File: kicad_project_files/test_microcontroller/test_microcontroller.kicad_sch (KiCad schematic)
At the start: 40 parts, among them J1 USB_C_Receptacle_USB2.0, SW1 SW_Push, SW2 SW_Push, SW3 SW_Push, SW4 SW_Push, SW5 SW_Push, SW6 SW_Push, SW7 SW_Push, SW8 SW_Push, SW9 SW_Push, U1 ATmega32U4-A, Y1 16mhz

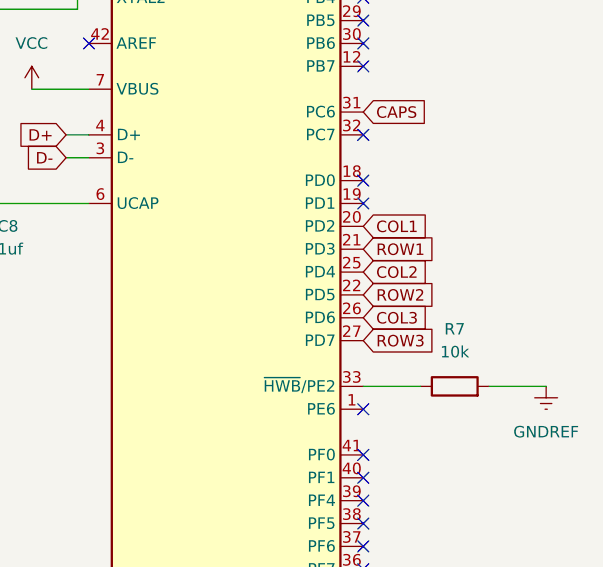
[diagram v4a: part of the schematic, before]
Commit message: add pcb traces
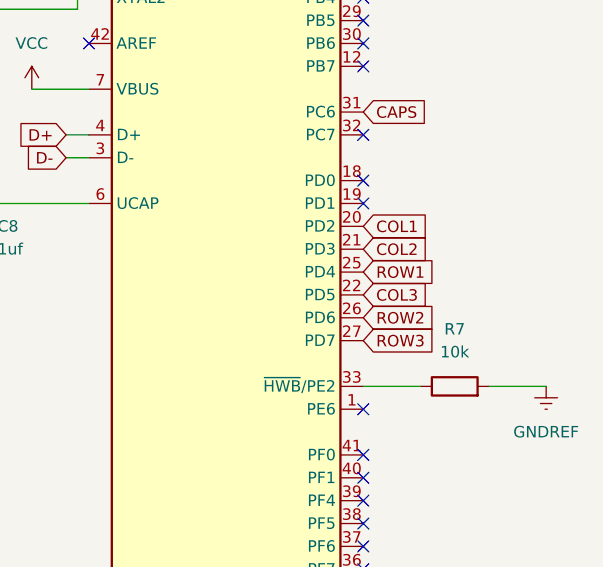
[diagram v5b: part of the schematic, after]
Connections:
- net COL2: now also U1.21 (PD3); no longer U1.25 (PD4)
- net COL3: now also U1.22 (PD5); no longer U1.26 (PD6)
- net ROW1: now also U1.25 (PD4); no longer U1.21 (PD3)
- net ROW2: now also U1.26 (PD6); no longer U1.22 (PD5)
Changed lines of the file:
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@@
+    )
+  )
+  (global_label "COL3" (shape input) (at 246.38 92.71 0) (fields_autoplaced)
+    (effects (font (size 1.27 1.27)) (justify left))
+    (property "Intersheet References" "${INTERSHEET_REFS}" (id 0) (at 253.6312 92.6306 0)
+      (effects (font (size 1.27 1.27)) (justify left) hide)
     )
   )
@@
     (effects (font (size 1.27 1.27)) (justify left))
     (property "Intersheet References" "${INTERSHEET_REFS}" (id 0) (at 183.0555 88.8206 0)
+      (effects (font (size 1.27 1.27)) (justify left) hide)
+    )
+  )
+  (global_label "ROW2" (shape input) (at 246.38 95.25 0) (fields_autoplaced)
+    (effects (font (size 1.27 1.27)) (justify left))
+    (property "Intersheet References" "${INTERSHEET_REFS}" (id 0) (at 254.0545 95.3294 0)
       (effects (font (size 1.27 1.27)) (justify left) hide)
     )
@@
     )
   )
-  (global_label "COL3" (shape input) (at 246.38 95.25 0) (fields_autoplaced)
-    (effects (font (size 1.27 1.27)) (justify left))
-    (property "Intersheet References" "${INTERSHEET_REFS}" (id 0) (at 253.6312 95.1706 0)
-      (effects (font (size 1.27 1.27)) (justify left) hide)
-    )
-  )
   (global_label "ROW2" (shape input) (at 33.02 128.27 180) (fields_autoplaced)
     (effects (font (size 1.27 1.27)) (justify right))
@@
     )
   )
-  (global_label "ROW2" (shape input) (at 246.38 92.71 0) (fields_autoplaced)
-    (effects (font (size 1.27 1.27)) (justify left))
-    (property "Intersheet References" "${INTERSHEET_REFS}" (id 0) (at 254.0545 92.7894 0)
-      (effects (font (size 1.27 1.27)) (justify left) hide)
-    )
-  )
   (global_label "D+" (shape input) (at 177.8 93.98 0) (fields_autoplaced)
     (effects (font (size 1.27 1.27)) (justify left))
@@
     (effects (font (size 1.27 1.27)) (justify left))
     (property "Intersheet References" "${INTERSHEET_REFS}" (id 0) (at 48.1806 76.5688 90)
+      (effects (font (size 1.27 1.27)) (justify left) hide)
+    )
+  )
+  (global_label "COL2" (shape input) (at 246.38 87.63 0) (fields_autoplaced)
+    (effects (font (size 1.27 1.27)) (justify left))
+    (property "Intersheet References" "${INTERSHEET_REFS}" (id 0) (at 253.6312 87.5506 0)
+      (effects (font (size 1.27 1.27)) (justify left) hide)
+    )
+  )
+  (global_label "ROW1" (shape input) (at 246.38 90.17 0) (fields_autoplaced)
+    (effects (font (size 1.27 1.27)) (justify left))
+    (property "Intersheet References" "${INTERSHEET_REFS}" (id 0) (at 254.0545 90.2494 0)
       (effects (font (size 1.27 1.27)) (justify left) hide)
     )
@@
     (effects (font (size 1.27 1.27)) (justify left))
     (property "Intersheet References" "${INTERSHEET_REFS}" (id 0) (at 253.3893 57.0706 0)
-      (effects (font (size 1.27 1.27)) (justify left) hide)
-    )
-  )
-  (global_label "ROW1" (shape input) (at 246.38 87.63 0) (fields_autoplaced)
-    (effects (font (size 1.27 1.27)) (justify left))
-    (property "Intersheet References" "${INTERSHEET_REFS}" (id 0) (at 254.0545 87.7094 0)
-      (effects (font (size 1.27 1.27)) (justify left) hide)
-    )
-  )
-  (global_label "COL2" (shape input) (at 246.38 90.17 0) (fields_autoplaced)
-    (effects (font (size 1.27 1.27)) (justify left))
-    (property "Intersheet References" "${INTERSHEET_REFS}" (id 0) (at 253.6312 90.0906 0)
       (effects (font (size 1.27 1.27)) (justify left) hide)
     )
@@
   (symbol (lib_id "power:PWR_FLAG") (at 148.59 115.57 0) (unit 1)
     (in_bom yes) (on_board yes) (fields_autoplaced)
-    (property "Reference" "#FLG?" (id 0) (at 148.59 113.665 0)
+    (property "Reference" "#FLG0102" (id 0) (at 148.59 113.665 0)
       (effects (font (size 1.27 1.27)) hide)
     )
@@
   (symbol (lib_id "power:PWR_FLAG") (at 158.75 69.85 0) (unit 1)
     (in_bom yes) (on_board yes) (fields_autoplaced)
-    (property "Reference" "#FLG?" (id 0) (at 158.75 67.945 0)
+    (property "Reference" "#FLG0101" (id 0) (at 158.75 67.945 0)
       (effects (font (size 1.27 1.27)) hide)
     )
@@
   )
   (symbol_instances
+    (path "/910bf9c7-3f9b-4ebb-810c-f11944d95f58"
+      (reference "#FLG0101") (unit 1) (value "PWR_FLAG") (footprint "")
+    )
     (path "/4d3913c1-6eaf-4788-b16d-404de55aea6d"
-      (reference "#FLG?") (unit 1) (value "PWR_FLAG") (footprint "")
-    )
-    (path "/910bf9c7-3f9b-4ebb-810c-f11944d95f58"
-      (reference "#FLG?") (unit 1) (value "PWR_FLAG") (footprint "")
+      (reference "#FLG0102") (unit 1) (value "PWR_FLAG") (footprint "")
     )
     (path "/51f6aabe-8284-47cf-8ddc-0d885dfc999b"

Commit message: complete traces
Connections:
- net GNDREF: now also ICSP_Programmer1.2 (Pin_2); no longer ICSP_Programmer1.6 (Pin_6)
- net MOSI: now also ICSP_Programmer1.3 (Pin_3); no longer ICSP_Programmer1.4 (Pin_4)
- net RESET: now also ICSP_Programmer1.4 (Pin_4); no longer ICSP_Programmer1.5 (Pin_5)
- net SCLK: now also ICSP_Programmer1.5 (Pin_5); no longer ICSP_Programmer1.3 (Pin_3)
- net VCC: now also ICSP_Programmer1.6 (Pin_6); no longer ICSP_Programmer1.2 (Pin_2)
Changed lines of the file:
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@@
   (no_connect (at 246.38 105.41))
   (no_connect (at 246.38 49.53))
-  (wire (pts (xy 130.81 50.8) (xy 130.81 52.07))
+  (wire (pts (xy 130.81 50.8) (xy 130.81 54.61))
     (stroke (width 0) (type default) (color 0 0 0 0))
   )
@@
     (stroke (width 0) (type default) (color 0 0 0 0))
   )
+  (wire (pts (xy 139.7 54.61) (xy 130.81 54.61))
+    (stroke (width 0) (type default) (color 0 0 0 0))
+  )
   (wire (pts (xy 36.83 29.21) (xy 40.64 29.21))
     (stroke (width 0) (type default) (color 0 0 0 0))
@@
     (stroke (width 0) (type default) (color 0 0 0 0))
   )
+  (wire (pts (xy 128.27 41.91) (xy 128.27 45.72))
+    (stroke (width 0) (type default) (color 0 0 0 0))
+  )
   (wire (pts (xy 33.02 149.86) (xy 38.1 149.86))
     (stroke (width 0) (type default) (color 0 0 0 0))
@@
     (stroke (width 0) (type default) (color 0 0 0 0))
   )
+  (wire (pts (xy 138.43 41.91) (xy 128.27 41.91))
+    (stroke (width 0) (type default) (color 0 0 0 0))
+  )
   (wire (pts (xy 134.62 113.03) (xy 134.62 116.84))
     (stroke (width 0) (type default) (color 0 0 0 0))
@@
   )
   (wire (pts (xy 163.83 90.17) (xy 163.83 88.9))
-    (stroke (width 0) (type default) (color 0 0 0 0))
-  )
-  (wire (pts (xy 128.27 45.72) (xy 133.35 45.72))
     (stroke (width 0) (type default) (color 0 0 0 0))
   )
@@
     )
   )
-  (global_label "SCLK" (shape input) (at 115.57 48.26 180) (fields_autoplaced)
-    (effects (font (size 1.27 1.27)) (justify right))
-    (property "Intersheet References" "${INTERSHEET_REFS}" (id 0) (at 108.3793 48.3394 0)
-      (effects (font (size 1.27 1.27)) (justify right) hide)
-    )
-  )
   (global_label "COL3" (shape input) (at 246.38 92.71 0) (fields_autoplaced)
     (effects (font (size 1.27 1.27)) (justify left))
@@
     (property "Intersheet References" "${INTERSHEET_REFS}" (id 0) (at 253.6312 85.0106 0)
       (effects (font (size 1.27 1.27)) (justify left) hide)
-    )
-  )
-  (global_label "RESET" (shape input) (at 115.57 50.8 180) (fields_autoplaced)
-    (effects (font (size 1.27 1.27)) (justify right))
-    (property "Intersheet References" "${INTERSHEET_REFS}" (id 0) (at 107.4117 50.7206 0)
-      (effects (font (size 1.27 1.27)) (justify right) hide)
     )
   )
@@
     )
   )
-  (global_label "MOSI" (shape input) (at 128.27 48.26 0) (fields_autoplaced)
-    (effects (font (size 1.27 1.27)) (justify left))
-    (property "Intersheet References" "${INTERSHEET_REFS}" (id 0) (at 135.2793 48.1806 0)
-      (effects (font (size 1.27 1.27)) (justify left) hide)
-    )
-  )
   (global_label "CAPS" (shape input) (at 101.6 22.86 180) (fields_autoplaced)
     (effects (font (size 1.27 1.27)) (justify right))
@@
     )
   )
+  (global_label "RESET" (shape input) (at 128.27 48.26 0) (fields_autoplaced)
+    (effects (font (size 1.27 1.27)) (justify left))
+    (property "Intersheet References" "${INTERSHEET_REFS}" (id 0) (at 136.4283 48.3394 0)
+      (effects (font (size 1.27 1.27)) (justify left) hide)
+    )
+  )
   (global_label "ROW1" (shape input) (at 246.38 90.17 0) (fields_autoplaced)
     (effects (font (size 1.27 1.27)) (justify left))
@@
     )
   )
+  (global_label "MOSI" (shape input) (at 115.57 48.26 180) (fields_autoplaced)
+    (effects (font (size 1.27 1.27)) (justify right))
+    (property "Intersheet References" "${INTERSHEET_REFS}" (id 0) (at 108.5607 48.3394 0)
+      (effects (font (size 1.27 1.27)) (justify right) hide)
+    )
+  )
+  (global_label "SCLK" (shape input) (at 115.57 50.8 180) (fields_autoplaced)
+    (effects (font (size 1.27 1.27)) (justify right))
+    (property "Intersheet References" "${INTERSHEET_REFS}" (id 0) (at 108.3793 50.8794 0)
+      (effects (font (size 1.27 1.27)) (justify right) hide)
+    )
+  )
   (global_label "MOSI" (shape input) (at 246.38 54.61 0) (fields_autoplaced)
     (effects (font (size 1.27 1.27)) (justify left))
@@
     )
     (property "Datasheet" "" (id 3) (at 209.55 69.85 0)
+      (effects (font (size 1.27 1.27)) hide)
+    )
+    (pin "1")
+  )
+  (symbol (lib_id "power:GNDREF") (at 138.43 41.91 0) (unit 1)
+    (in_bom yes) (on_board yes) (fields_autoplaced)
+    (property "Reference" "#PWR?" (id 0) (at 138.43 48.26 0)
+      (effects (font (size 1.27 1.27)) hide)
+    )
+    (property "Value" "GNDREF" (id 1) (at 138.43 46.99 0))
+    (property "Footprint" "" (id 2) (at 138.43 41.91 0)
+      (effects (font (size 1.27 1.27)) hide)
+    )
+    (property "Datasheet" "" (id 3) (at 138.43 41.91 0)
       (effects (font (size 1.27 1.27)) hide)
     )
@@
     (pin "2")
   )
-  (symbol (lib_id "power:VCC") (at 133.35 45.72 0) (unit 1)
-    (in_bom yes) (on_board yes) (fields_autoplaced)
-    (property "Reference" "#PWR017" (id 0) (at 133.35 49.53 0)
-      (effects (font (size 1.27 1.27)) hide)
-    )
-    (property "Value" "VCC" (id 1) (at 133.35 40.64 0))
-    (property "Footprint" "" (id 2) (at 133.35 45.72 0)
-      (effects (font (size 1.27 1.27)) hide)
-    )
-    (property "Datasheet" "" (id 3) (at 133.35 45.72 0)
-      (effects (font (size 1.27 1.27)) hide)
-    )
-    (pin "1")
-  )
   (symbol (lib_id "Diode:1N4148") (at 77.47 124.46 90) (unit 1)
     (in_bom yes) (on_board yes) (fields_autoplaced)
@@
     (pin "1")
   )
-  (symbol (lib_id "power:GNDREF") (at 130.81 52.07 0) (unit 1)
-    (in_bom yes) (on_board yes) (fields_autoplaced)
-    (property "Reference" "#PWR016" (id 0) (at 130.81 58.42 0)
-      (effects (font (size 1.27 1.27)) hide)
-    )
-    (property "Value" "GNDREF" (id 1) (at 130.81 57.15 0))
-    (property "Footprint" "" (id 2) (at 130.81 52.07 0)
-      (effects (font (size 1.27 1.27)) hide)
-    )
-    (property "Datasheet" "" (id 3) (at 130.81 52.07 0)
-      (effects (font (size 1.27 1.27)) hide)
-    )
-    (pin "1")
-  )
   (symbol (lib_id "power:VCC") (at 231.14 35.56 0) (unit 1)
     (in_bom yes) (on_board yes) (fields_autoplaced)
@@
     (pin "2")
   )
+  (symbol (lib_id "power:VCC") (at 139.7 54.61 0) (unit 1)
+    (in_bom yes) (on_board yes) (fields_autoplaced)
+    (property "Reference" "#PWR?" (id 0) (at 139.7 58.42 0)
+      (effects (font (size 1.27 1.27)) hide)
+    )
+    (property "Value" "VCC" (id 1) (at 139.7 49.53 0))
+    (property "Footprint" "" (id 2) (at 139.7 54.61 0)
+      (effects (font (size 1.27 1.27)) hide)
+    )
+    (property "Datasheet" "" (id 3) (at 139.7 54.61 0)
+      (effects (font (size 1.27 1.27)) hide)
+    )
+    (pin "1")
+  )
   (symbol (lib_id "Switch:SW_Push") (at 31.75 29.21 0) (unit 1)
     (in_bom yes) (on_board yes) (fields_autoplaced)
@@
       (reference "#PWR014") (unit 1) (value "GNDREF") (footprint "")
     )
-    (path "/6f9440f8-a9f0-42af-bfc6-f816927170e2"
-      (reference "#PWR016") (unit 1) (value "GNDREF") (footprint "")
-    )
-    (path "/25d8ce34-f34b-4496-8900-e9d2598324a2"
-      (reference "#PWR017") (unit 1) (value "VCC") (footprint "")
-    )
     (path "/a717bee7-1902-40ae-b673-fad1ccbf129c"
       (reference "#PWR0101") (unit 1) (value "GNDREF") (footprint "")
     )
+    (path "/0db4c658-cce5-4054-86a1-1dda33675c26"
+      (reference "#PWR?") (unit 1) (value "GNDREF") (footprint "")
+    )
+    (path "/d26e8902-207a-45d3-9cc8-035ef9ae29e9"
+      (reference "#PWR?") (unit 1) (value "VCC") (footprint "")
+    )
     (path "/4d48e41d-3878-4a27-ab4f-51a7ebfea6fe"

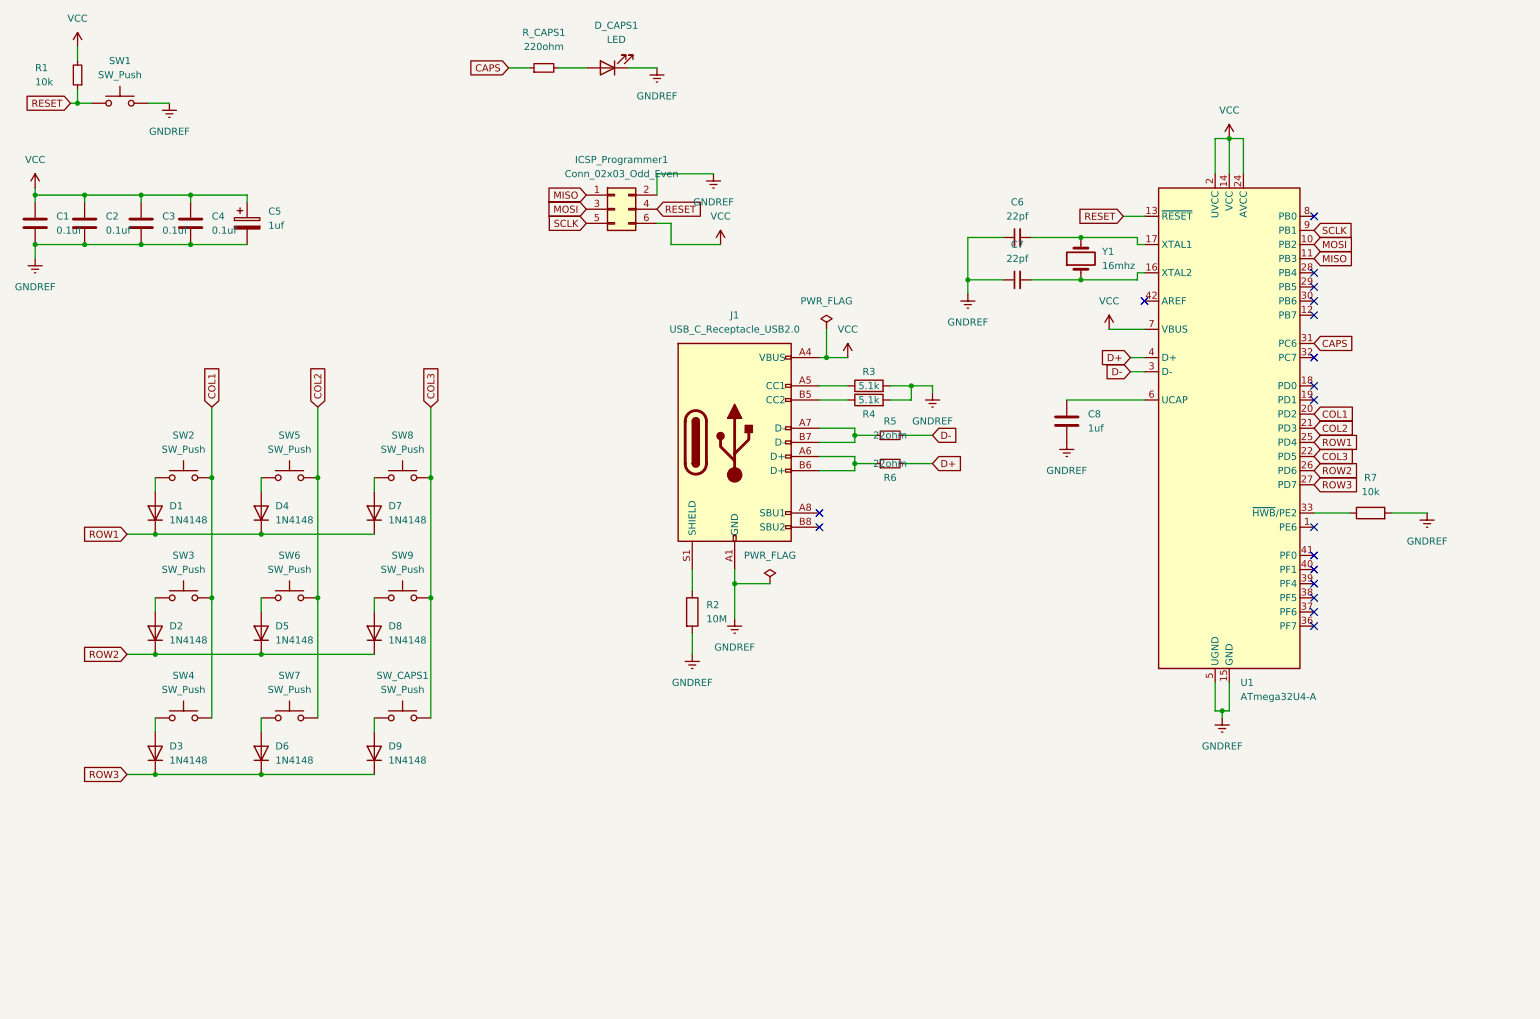
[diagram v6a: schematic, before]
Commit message: add new mcu and voltage regulator
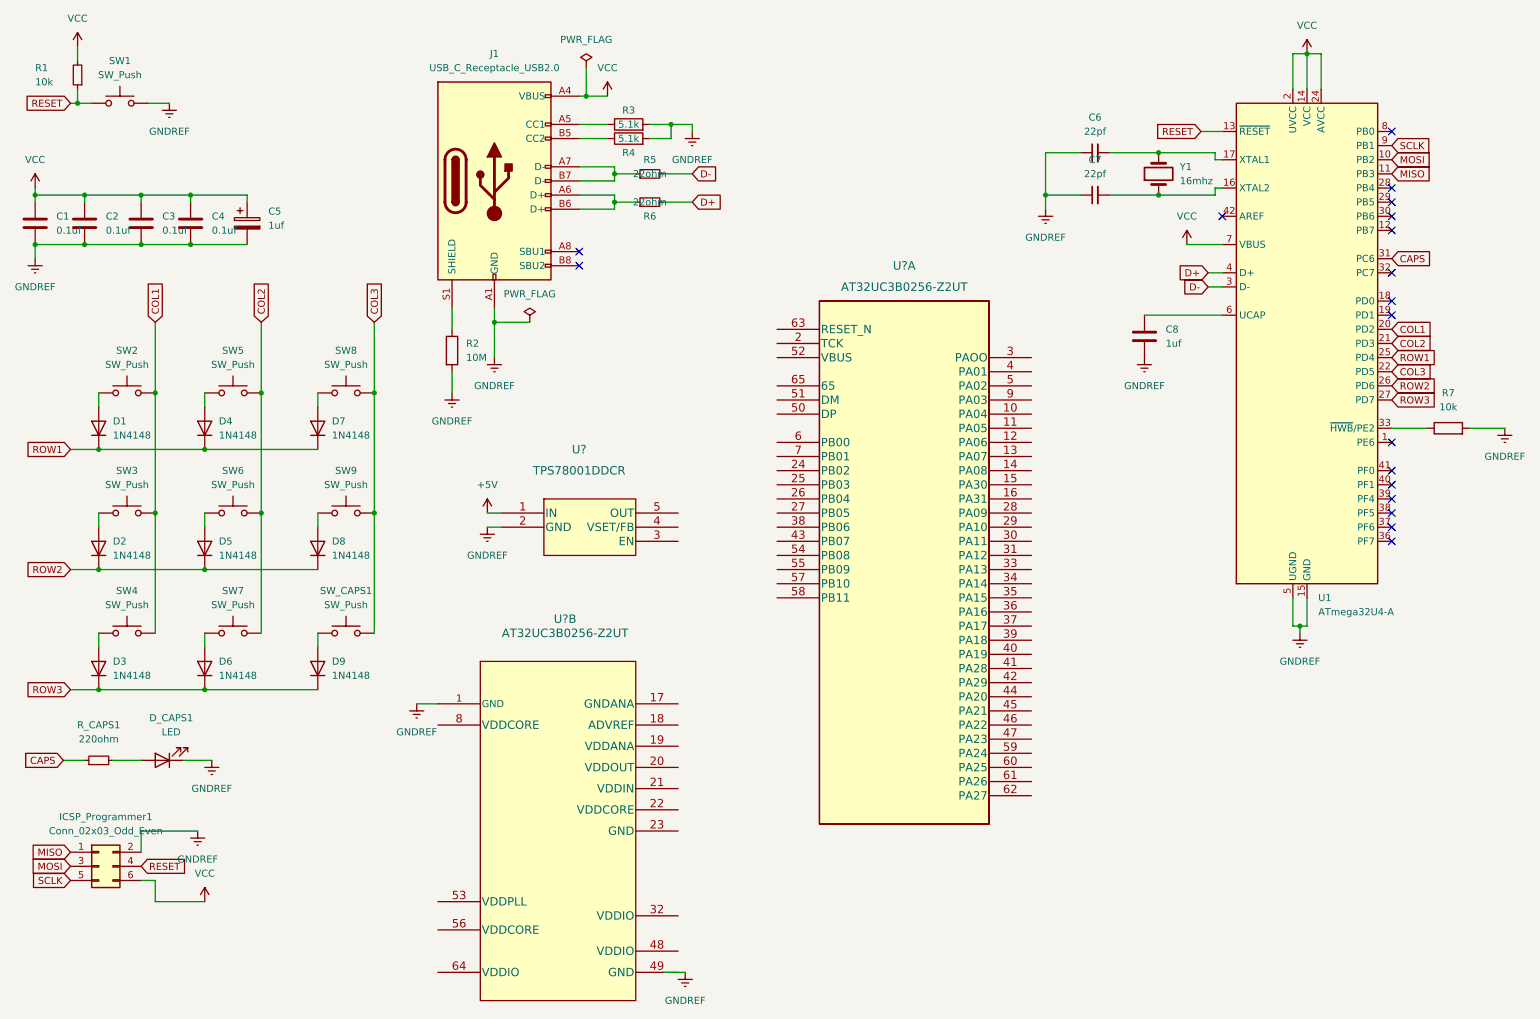
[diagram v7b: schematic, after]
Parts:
- added U? (x2): AT32UC3B0256-Z2UT, QFN64-4_ATM, symbol AT32UC3B0256-Z2UT:AT32UC3B0256-Z2UT
- added U?: TPS78001DDCR, DDC5, symbol TPS780xx:TPS78001DDCR
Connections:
- net GNDREF: now also U?.1 (GND), U?.2 (GND)
- new net +5V: U?.1 (IN)
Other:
- moved on the sheet: C6, C7, C8, D1, D2, D3, D4, D5, D6, D7, D8, D9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
